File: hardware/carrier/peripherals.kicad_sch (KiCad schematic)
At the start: 25 parts, among them J4 CARDKB, J5 FRONTLIGHT, J6 MSG_LED, J7 HAPTIC, Q4 2N7002, U7 LIS2DW12TR, U8 NSI45020AT1G, U9 DRV2605LDGSR

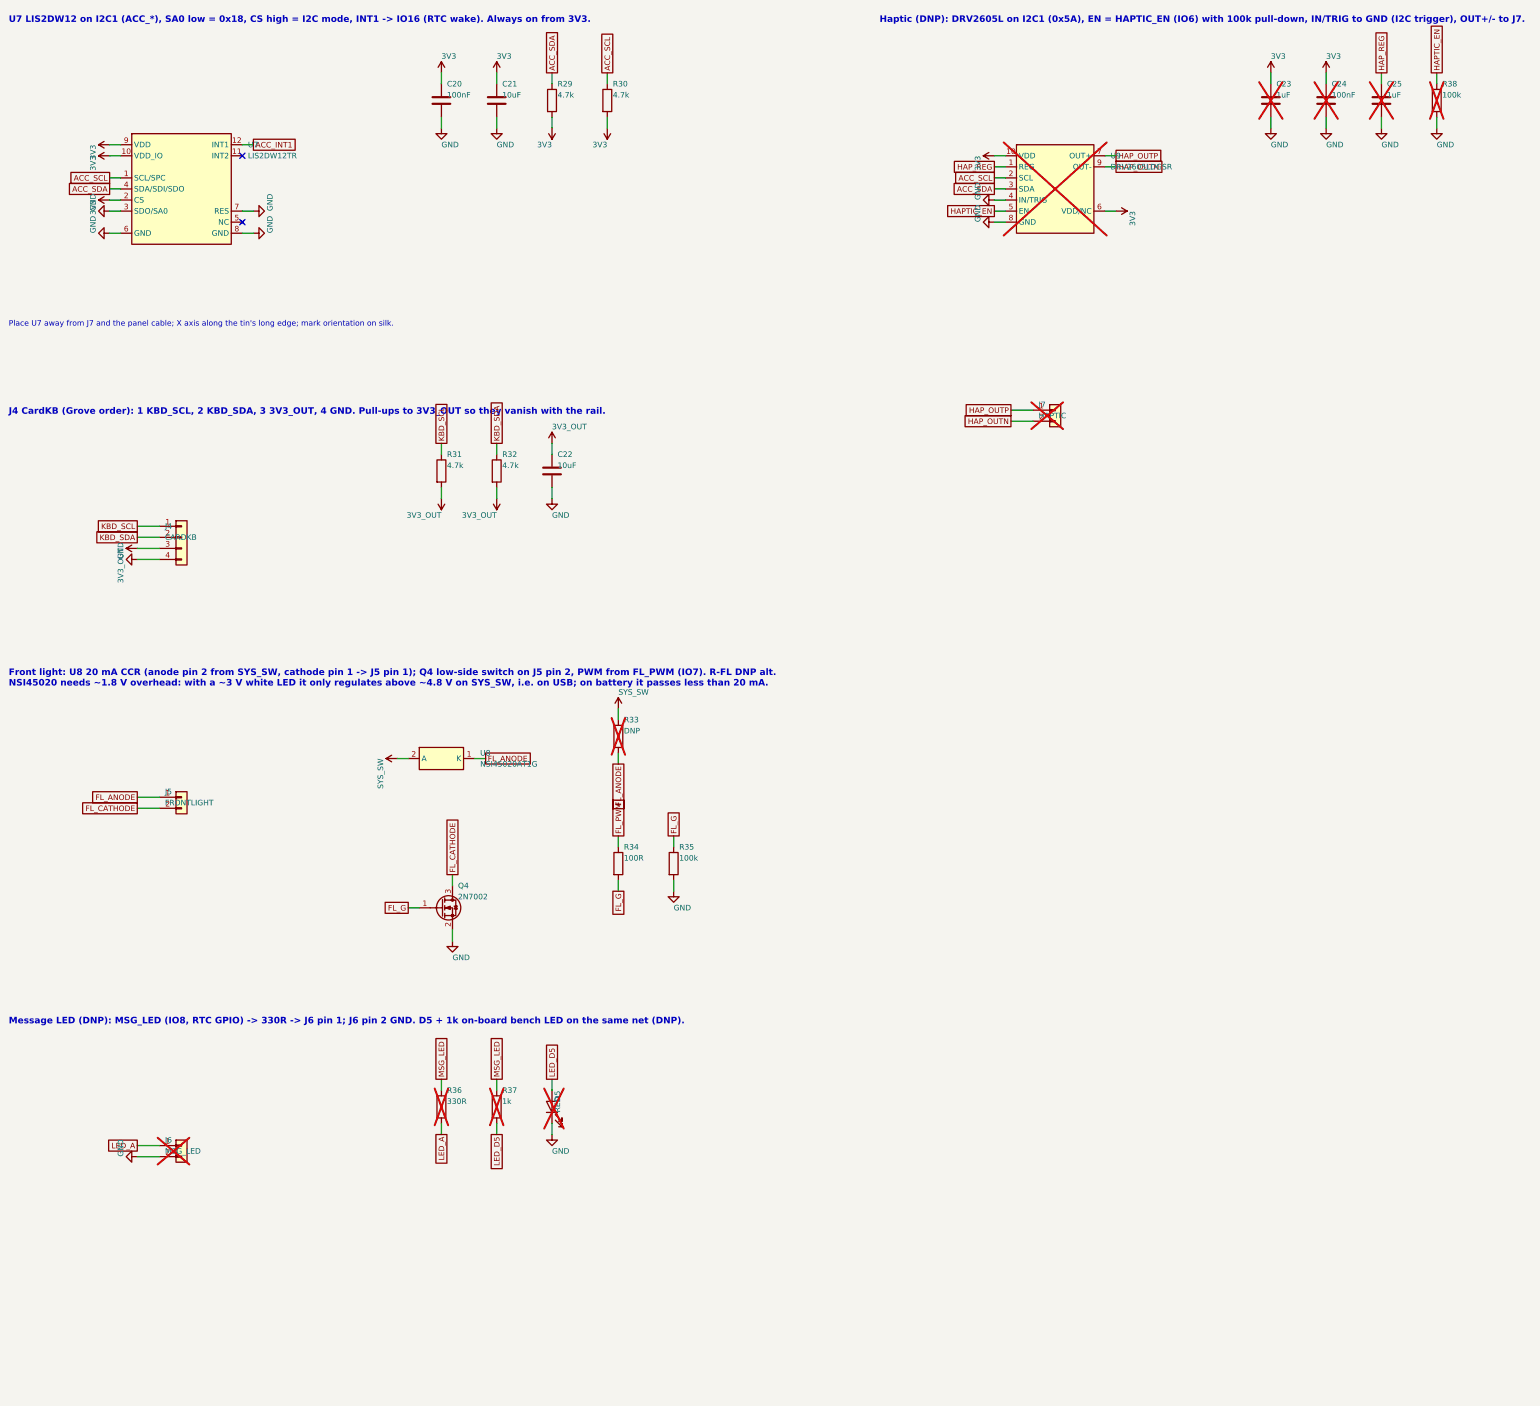
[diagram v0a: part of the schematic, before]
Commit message: hardware/carrier: front light is the GDEY029T94-FL03 (6-pin flex -> FH34SRJ-6S on the panel board, anode/cathode over a 10-way SH cable, 33R 1206 + Q4 PWM drive replaces the NSI45020), front-light button SW2 on IO4 (FL_BTN), low-profile pass (FH34SRJ 1.0 mm ZIFs, 2 x 100uF 0805 instead of the 2.5 mm 1210, part-height table), sleep-current audit (Q1 gate pull-up 100k -> 2.2M: 38 -> 1.9 uA; SN74LVC2G126 moved to the bus-powered BRG_VDD rail: 0 on battery; table in the README), TPS62840 has no fixed-3.3 V variant (README). Custom FH34SRJ footprints from the Hirose catalog; LCSC numbers via the JLCPCB parts API. Both boards re-placed and re-routed: 0 unconnected, 0 clearance/courtyard errors, silk notes only; ERC 0/0; exports refreshed (owner, 17 Oct 2026)
Co-Authored-By: Claude Fable 5.1 <noreply@anthropic.com>
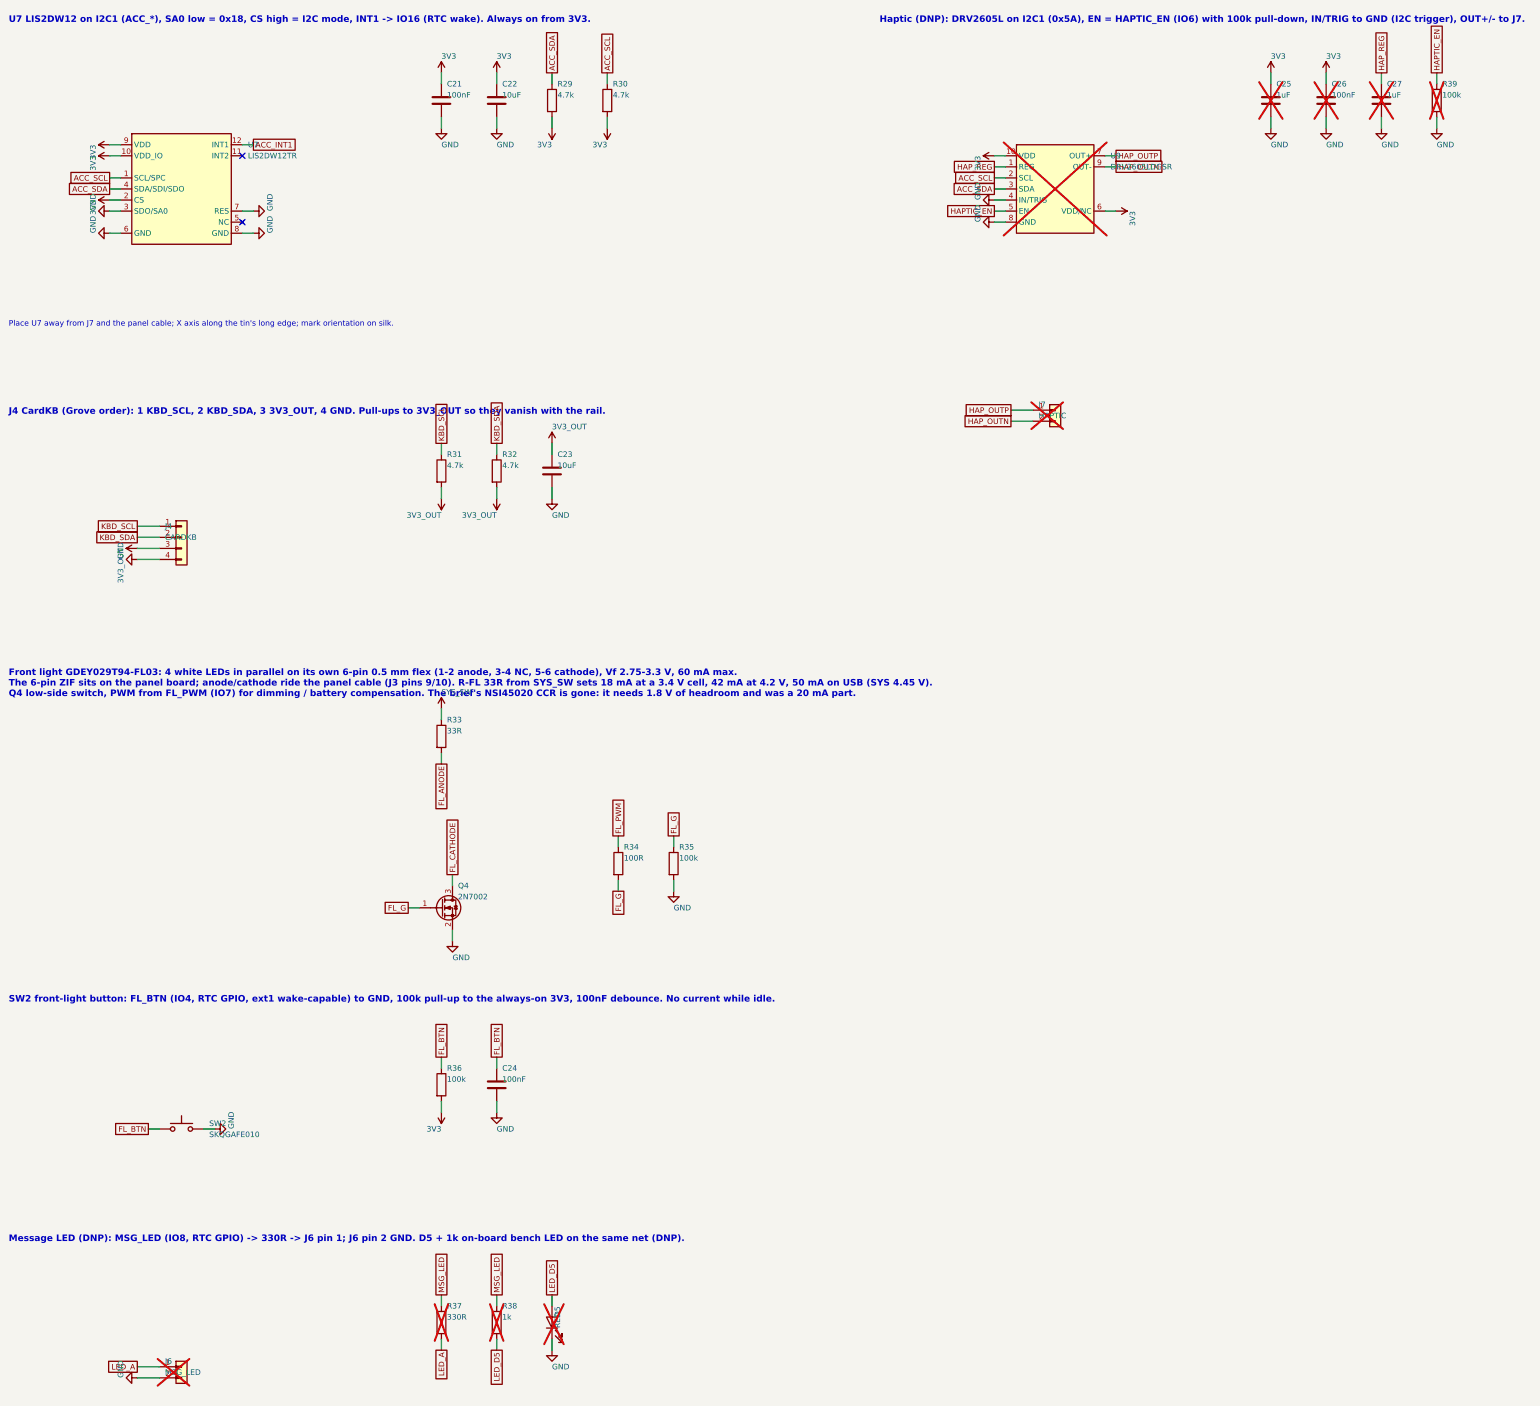
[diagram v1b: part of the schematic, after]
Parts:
- removed C20: 100nF, Capacitor_SMD:C_0603_1608Metric, symbol Device:C
- removed J5: FRONTLIGHT, Connector_JST:JST_SH_SM02B-SRSS-TB_1x02-1MP_P1.00mm_Horizontal, symbol Connector_Generic:Conn_01x02
- removed U8: NSI45020AT1G, Diode_SMD:D_SOD-123, symbol pager-carrier:NSI45020AT1G
- added C26: 100nF, Capacitor_SMD:C_0603_1608Metric, symbol Device:C
- added C27: 1uF, Capacitor_SMD:C_0603_1608Metric, symbol Device:C
- added R39: 100k, Resistor_SMD:R_0603_1608Metric, symbol Device:R
- added SW2: SKQGAFE010, Button_Switch_SMD:SW_SPST_SKQG_WithoutStem, symbol Switch:SW_Push
- C21: value 10uF -> 100nF; LCSC C19702 -> C14663; MPN CL10A106KP8NNNC -> CL10B104KB8NNNC
- C23: value 1uF -> 10uF; DNP DNP -> (none); LCSC C15849 -> C19702; MPN CL10A105KA8NNNC -> CL10A106KP8NNNC; now fitted
- C24: DNP DNP -> (none); now fitted
- R33: value DNP -> 33R; footprint Resistor_SMD:R_0603_1608Metric -> Resistor_SMD:R_1206_3216Metric; DNP DNP -> (none); LCSC (none) -> C18005; MPN (none) -> 1206W4F330JT5E; Note R-FL: series resistor alternative to U8 -> R-FL, 1206 for 0.1 W at 50 mA; lower for a brighter light, 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; now fitted
- R36: value 330R -> 100k; DNP DNP -> (none); LCSC C23138 -> C25803; MPN 0603WAF3300T5E -> 0603WAF1003T5E; now fitted
- R37: value 1k -> 330R; LCSC C21190 -> C23138; MPN 0603WAF1001T5E -> 0603WAF3300T5E
- R38: value 100k -> 1k; LCSC C25803 -> C21190; MPN 0603WAF1003T5E -> 0603WAF1001T5E
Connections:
- net 3V3: now also C22.1, C25.1, R36.2, C26.1; no longer C23.1, C24.1
- net 3V3_OUT: now also C23.1; no longer C22.1
- net GND: now also C26.2, C27.2, R39.2, SW2.2; no longer R38.2
- net HAPTIC_EN: now also R39.1; no longer R38.1
- net HAP_REG: now also C27.1; no longer C25.1
- net LED_A: now also R37.2; no longer R36.2
- net LED_D5: now also R38.2; no longer R37.2
- net MSG_LED: now also R38.1; no longer R36.1
- new net FL_BTN: C24.1, R36.1, SW2.1
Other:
- note added: "Front light GDEY029T94-FL03: 4 white LEDs in parallel on its own 6-pin 0.5 mm flex (1-2 anode, 3-4 NC, 5-6 cathode), Vf 2.75-3.3 V, 60 mA max. The 6-pin ZIF sits on the panel board; anode/cathode ride the panel cable (J3 pins 9/10). R-FL 33R from SYS_SW sets 18 mA at a 3.4 V cell, 42 mA at 4.2 V, 50 mA on USB (SYS 4.45 V). Q4 low-side switch, PWM from FL_PWM (IO7) for dimming / battery compensati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"
- note added: "SW2 front-light button: FL_BTN (IO4, RTC GPIO, ext1 wake-capable) to GND, 100k pull-up to the always-on 3V3, 100nF debounce. No current while idle."
- note removed: "Front light: U8 20 mA CCR (anode pin 2 from SYS_SW, cathode pin 1 -> J5 pin 1); Q4 low-side switch on J5 pin 2, PWM from FL_PWM (IO7). R-FL DNP alt. NSI45020 needs ~1.8 V overhead: with a ~3 V white LED it only regulates above ~4.8 V on SYS_SW, i.e. on USB; on battery it passes less than 20 mA."
- moved on the sheet: C21, C22, C25, D5, J6, R37, R38
